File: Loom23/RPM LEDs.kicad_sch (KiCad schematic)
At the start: 0 parts

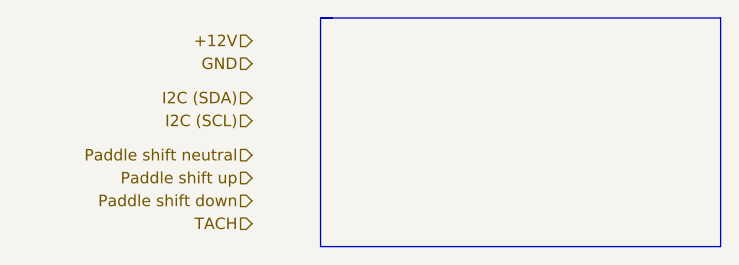
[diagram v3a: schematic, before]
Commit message: Added paddle shifter PCB and the relays.
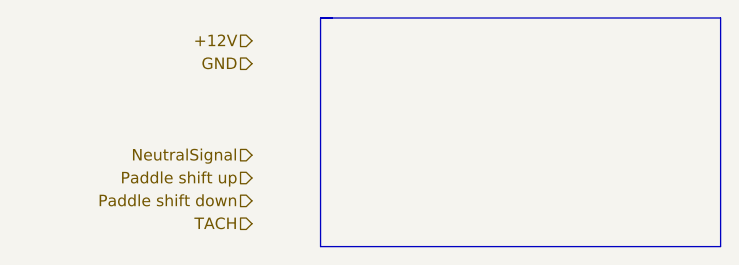
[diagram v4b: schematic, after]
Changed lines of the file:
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@@
-    (effects (font (size 1.27 1.27)) (justify right))
-  )
-  (hierarchical_label "I2C (SDA)" (shape input) (at 92.71 114.3 180)
     (effects (font (size 1.27 1.27)) (justify right))
   )
@@
     (effects (font (size 1.27 1.27)) (justify right))
   )
-  (hierarchical_label "I2C (SCL)" (shape input) (at 92.71 116.84 180)
-    (effects (font (size 1.27 1.27)) (justify right))
-  )
   (hierarchical_label "Paddle shift up" (shape input) (at 92.71 123.19 180)
     (effects (font (size 1.27 1.27)) (justify right))
   )
-  (hierarchical_label "Paddle shift neutral" (shape input) (at 92.71 120.65 180)
+  (hierarchical_label "NeutralSignal" (shape input) (at 92.71 120.65 180)
     (effects (font (size 1.27 1.27)) (justify right))
   )

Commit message: Added brake light
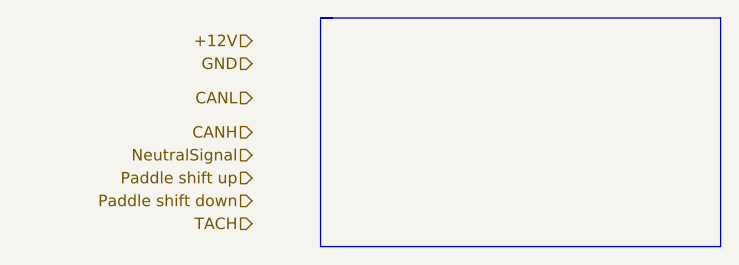
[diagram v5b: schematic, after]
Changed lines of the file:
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@@
+    (effects (font (size 1.27 1.27)) (justify right))
+  )
+  (hierarchical_label "CANL" (shape input) (at 92.71 114.3 180)
     (effects (font (size 1.27 1.27)) (justify right))
   )
@@
     (effects (font (size 1.27 1.27)) (justify right))
   )
+  (hierarchical_label "CANH" (shape input) (at 92.71 118.11 180)
+    (effects (font (size 1.27 1.27)) (justify right))
+  )
